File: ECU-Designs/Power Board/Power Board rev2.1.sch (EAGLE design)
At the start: 56 parts, among them X1 MINIFIT_5566-2, X2 MINIFIT_5566-6

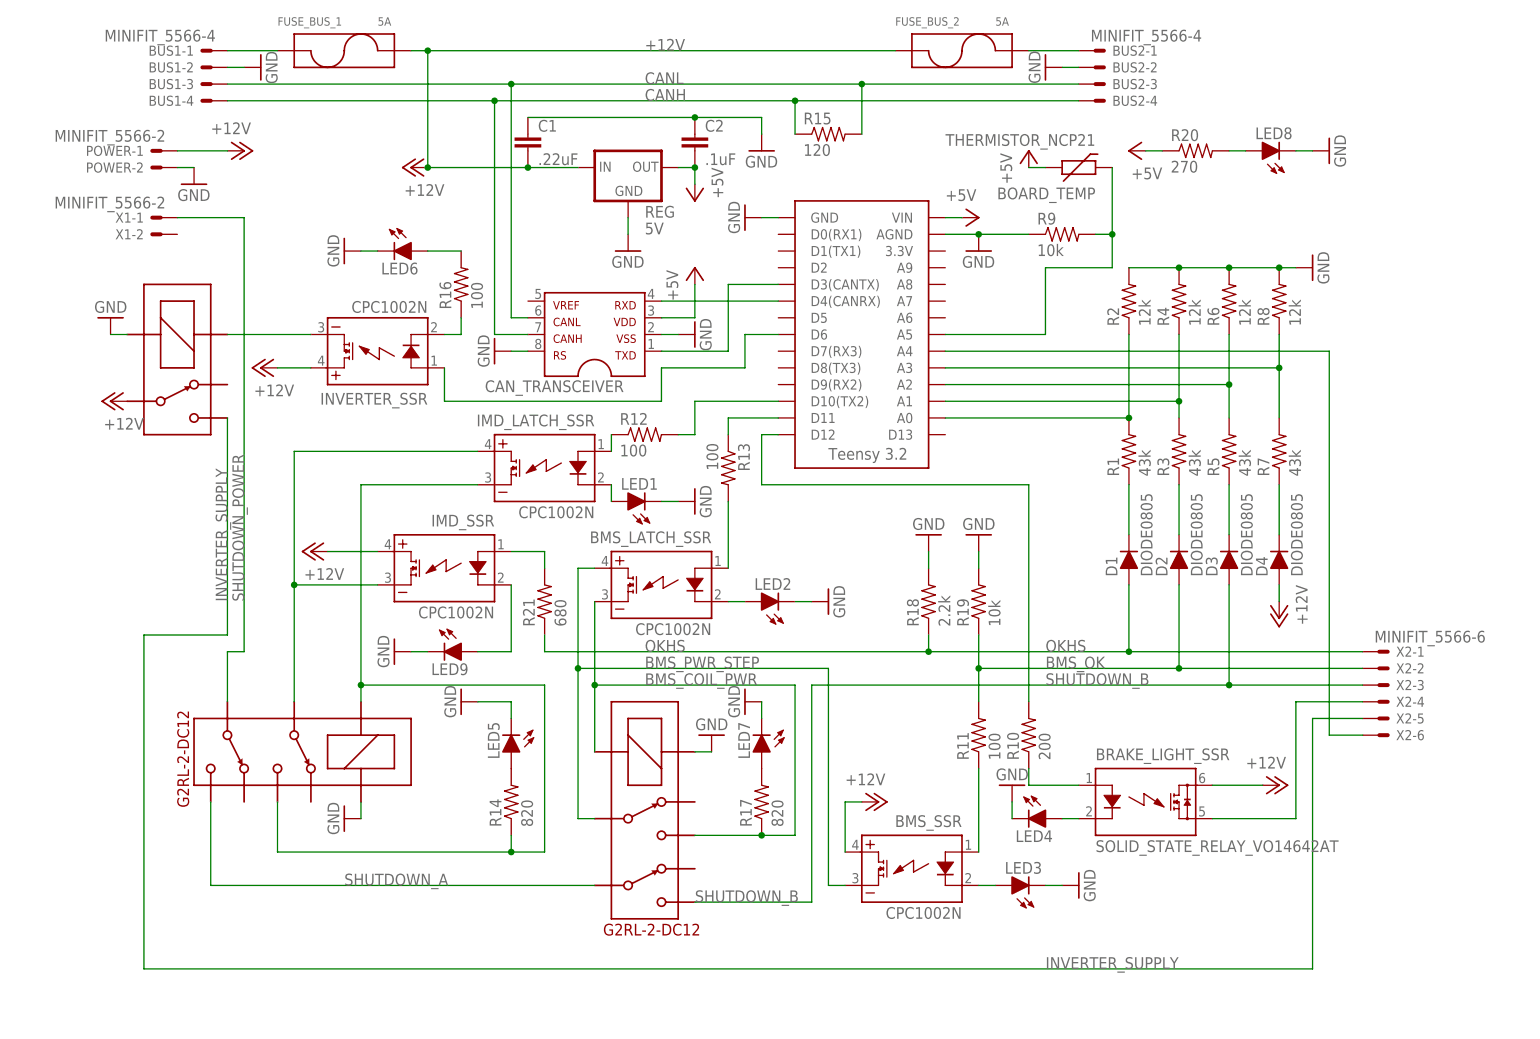
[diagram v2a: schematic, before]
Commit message: Power board: add gnd, remove unneeded diode; External diagram: update HV PCB wiring and power board wiring; HV board: changes to meet rules, clearer HV naming, remove microcontroller
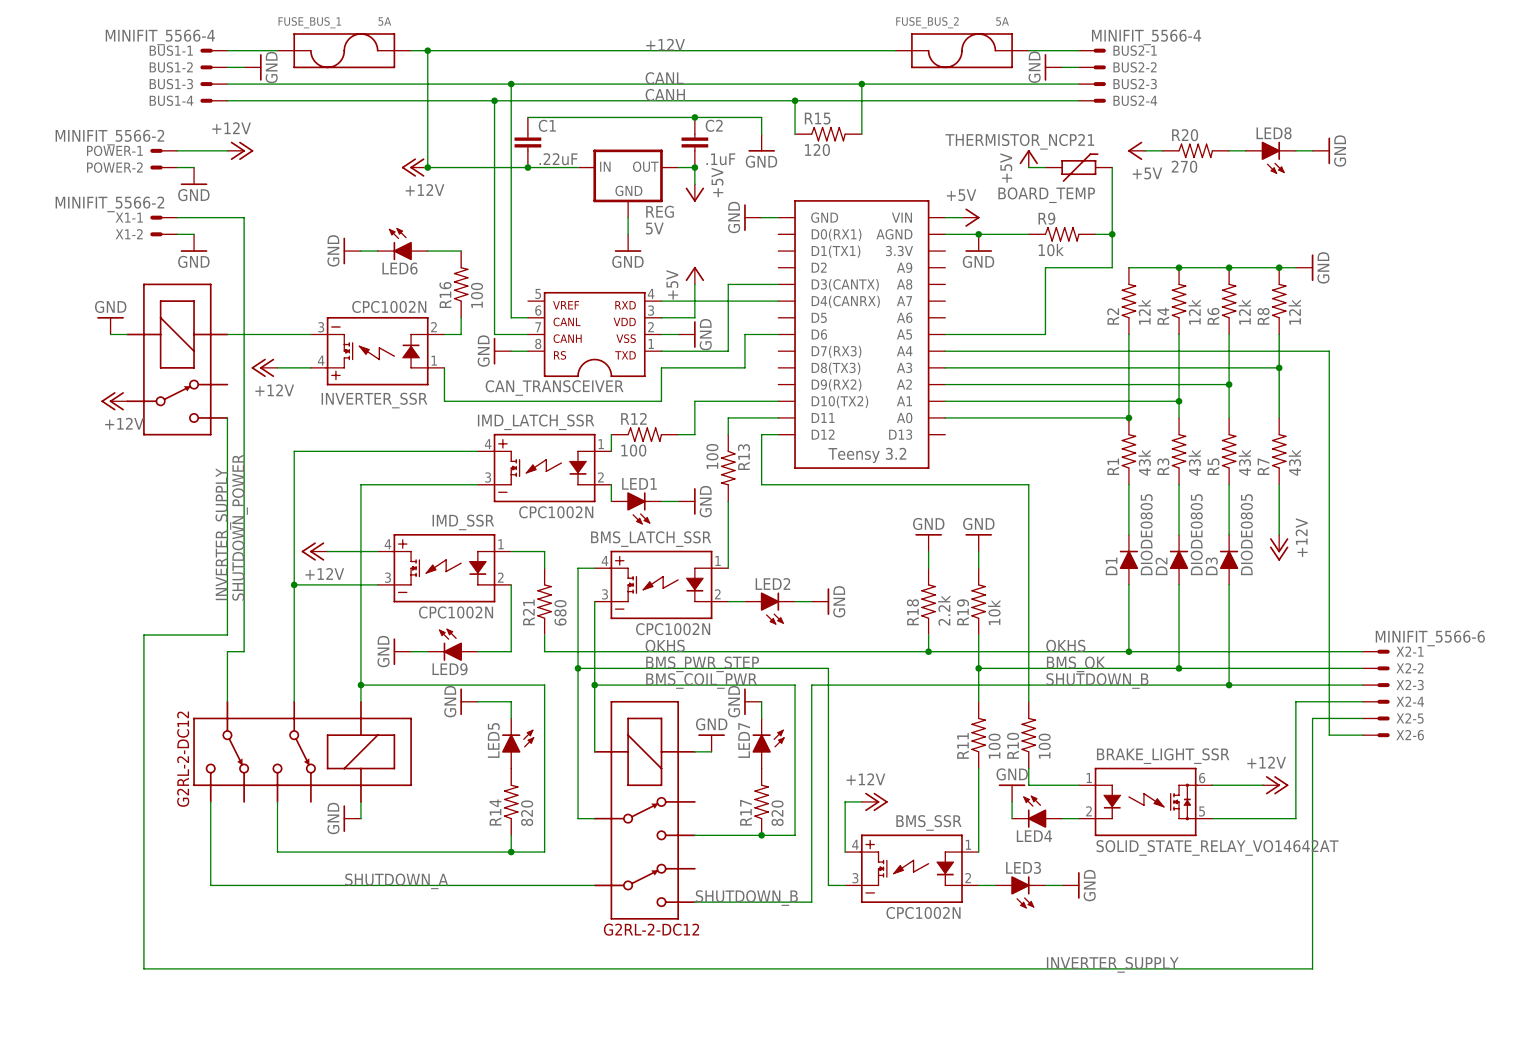
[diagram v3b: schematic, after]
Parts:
- removed D4: DIODE0805, HyTechDevices:DIODE0805
- R10: value 200 -> 100
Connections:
- net N$10 renamed 12V_F1
- net N$11 renamed 12V_F2
- removed net N$25: D4.C, R7.1
- net +12V: now also R7.1; no longer D4.A
- net GND: now also X1-2.S
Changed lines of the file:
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@@
 <part name="BOARD_TEMP" library="HyTechDevices" deviceset="THERMISTOR_NCP21" device=""/>
 <part name="R9" library="HyTechDevices" deviceset="RESISTOR" device="0805-RES" value="10k"/>
-<part name="R10" library="HyTechDevices" deviceset="RESISTOR" device="0805-RES" value="200"/>
+<part name="R10" library="HyTechDevices" deviceset="RESISTOR" device="0805-RES" value="100"/>
 <part name="R11" library="HyTechDevices" deviceset="RESISTOR" device="0805-RES" value="100"/>
 <part name="R12" library="HyTechDevices" deviceset="RESISTOR" device="0805-RES" value="100"/>
@@
 <part name="D2" library="HyTechDevices" deviceset="DIODE" device="0805"/>
 <part name="D3" library="HyTechDevices" deviceset="DIODE" device="0805"/>
-<part name="D4" library="HyTechDevices" deviceset="DIODE" device="0805"/>
 <part name="INVERTER_SSR" library="HyTechDevices" deviceset="CPC1002N" device=""/>
 <part name="LED6" library="HyTechDevices" deviceset="LED" device="-0805"/>
@@
 <part name="P+5" library="supply1" deviceset="+12V" device=""/>
 <part name="X1" library="HyTechDevices" deviceset="MINIFIT_5566-2" device=""/>
+<part name="GND25" library="HyTechSymbols" deviceset="GND" device=""/>
 </parts>
 <sheets>
@@
 <instance part="D2" gate="1" x="147.32" y="50.8" rot="R90"/>
 <instance part="D3" gate="1" x="154.94" y="50.8" rot="R90"/>
-<instance part="D4" gate="1" x="162.56" y="50.8" rot="R90"/>
 <instance part="INVERTER_SSR" gate="G$1" x="25.4" y="81.28" rot="R180"/>
 <instance part="LED6" gate="LED" x="30.48" y="96.52" rot="R270"/>
@@
 <instance part="P+10" gate="1" x="15.24" y="50.8" rot="R90"/>
 <instance part="P+12" gate="1" x="162.56" y="15.24" rot="R270"/>
-<instance part="P+13" gate="1" x="162.56" y="40.64" rot="R180"/>
+<instance part="P+13" gate="1" x="162.56" y="50.8" rot="R180"/>
 <instance part="P+14" gate="1" x="30.48" y="109.22" rot="R90"/>
 <instance part="P+5" gate="1" x="101.6" y="12.7" rot="R270"/>
 <instance part="X1" gate="-2" x="-7.62" y="99.06" rot="MR0"/>
 <instance part="X1" gate="-1" x="-7.62" y="101.6" rot="MR0"/>
+<instance part="GND25" gate="1" x="-2.54" y="96.52"/>
 </instances>
 <busses>
@@
 <pinref part="GND24" gate="1" pin="GND"/>
 <wire x1="33.02" y1="35.56" x2="30.48" y2="35.56" width="0.1524" layer="91"/>
+</segment>
+<segment>
+<pinref part="X1" gate="-2" pin="S"/>
+<pinref part="GND25" gate="1" pin="GND"/>
+<wire x1="-2.54" y1="99.06" x2="-5.08" y2="99.06" width="0.1524" layer="91"/>
 </segment>
 </net>
@@
 </segment>
 </net>
-<net name="N$10" class="0">
+<net name="12V_F1" class="0">
 <segment>
 <pinref part="FUSE_BUS_1" gate="G$1" pin="P1"/>
@@
 </segment>
 </net>
-<net name="N$11" class="0">
+<net name="12V_F2" class="0">
 <segment>
 <pinref part="FUSE_BUS_2" gate="G$1" pin="P2"/>
@@
 </segment>
 </net>
-<net name="N$25" class="0">
-<segment>
-<pinref part="R7" gate="G$1" pin="1"/>
-<wire x1="162.56" y1="60.96" x2="162.56" y2="53.34" width="0.1524" layer="91"/>
-<pinref part="D4" gate="1" pin="C"/>
-</segment>
-</net>
 <net name="N$26" class="0">
 <segment>
@@
 </segment>
 <segment>
-<pinref part="D4" gate="1" pin="A"/>
 <pinref part="P+13" gate="1" pin="+12V"/>
-<wire x1="162.56" y1="43.18" x2="162.56" y2="45.72" width="0.1524" layer="91"/>
-</segment>
-<segment>
+<pinref part="R7" gate="G$1" pin="1"/>
+<wire x1="162.56" y1="60.96" x2="162.56" y2="53.34" width="0.1524" layer="91"/>
+</segment>
+<segment>
